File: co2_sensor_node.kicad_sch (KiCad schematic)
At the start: 27 parts, among them J1 Conn_01x03, J2 Conn_01x03, J3 Conn_01x02, J4 Conn_01x02, J5 Conn_01x03, J6 Conn_01x03

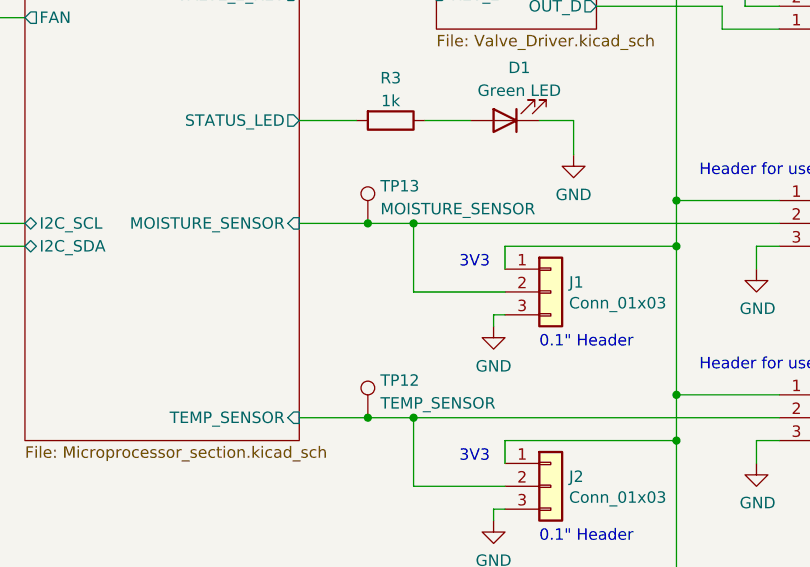
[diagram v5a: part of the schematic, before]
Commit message: Add voltage selection header for fan
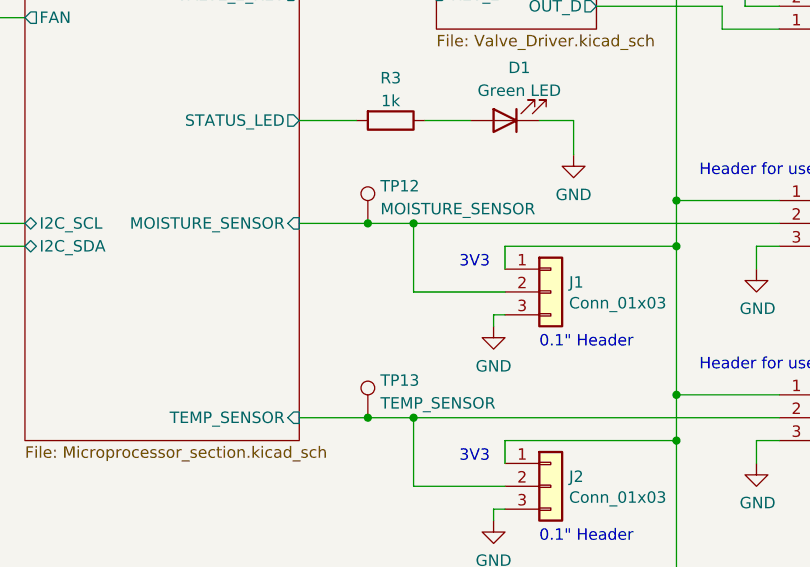
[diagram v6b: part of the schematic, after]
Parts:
- renumbered TP13 to TP12, TP12 to TP13
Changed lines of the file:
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@@
   (symbol (lib_id "Connector:TestPoint") (at 167.64 115.57 0) (unit 1)
     (in_bom yes) (on_board yes) (fields_autoplaced)
-    (property "Reference" "TP12" (id 0) (at 169.037 111.4333 0)
+    (property "Reference" "TP13" (id 0) (at 169.037 111.4333 0)
       (effects (font (size 1.27 1.27)) (justify left))
     )
@@
   (symbol (lib_id "Connector:TestPoint") (at 167.64 93.98 0) (unit 1)
     (in_bom yes) (on_board yes) (fields_autoplaced)
-    (property "Reference" "TP13" (id 0) (at 169.037 89.8433 0)
+    (property "Reference" "TP12" (id 0) (at 169.037 89.8433 0)
       (effects (font (size 1.27 1.27)) (justify left))
     )
@@
       (reference "#PWR039") (unit 1) (value "GND") (footprint "")
     )
+    (path "/00000000-0000-0000-0000-000060d4d720/a2b76130-4b73-41d2-b95d-ad9995d504d5"
+      (reference "#PWR040") (unit 1) (value "+BATT") (footprint "")
+    )
     (path "/00000000-0000-0000-0000-000060d4d720/00000000-0000-0000-0000-000060d47c8b"
-      (reference "#PWR040") (unit 1) (value "GND") (footprint "")
+      (reference "#PWR041") (unit 1) (value "GND") (footprint "")
     )
     (path "/1e0f6ce1-838d-48f3-88cf-c2592ace5fc7/78d904c8-e560-4928-a784-d6fb19cbf40d"
-      (reference "#PWR041") (unit 1) (value "GND") (footprint "")
+      (reference "#PWR042") (unit 1) (value "GND") (footprint "")
     )
     (path "/1e0f6ce1-838d-48f3-88cf-c2592ace5fc7/cbc2d777-8f3b-4a67-809c-e3f7baeb774b"
-      (reference "#PWR042") (unit 1) (value "GND") (footprint "")
+      (reference "#PWR043") (unit 1) (value "GND") (footprint "")
     )
     (path "/1e0f6ce1-838d-48f3-88cf-c2592ace5fc7/5cc37d78-3060-40cb-84bf-6df8015e864f"
-      (reference "#PWR043") (unit 1) (value "GND") (footprint "")
+      (reference "#PWR044") (unit 1) (value "GND") (footprint "")
     )
     (path "/1e0f6ce1-838d-48f3-88cf-c2592ace5fc7/b321f6d2-0341-4b1f-bee3-66cbe5374b62"
-      (reference "#PWR044") (unit 1) (value "GND") (footprint "")
+      (reference "#PWR045") (unit 1) (value "GND") (footprint "")
     )
     (path "/00000000-0000-0000-0000-000060a7e012/00000000-0000-0000-0000-000060a80f45"
-      (reference "#PWR045") (unit 1) (value "GND") (footprint "")
+      (reference "#PWR046") (unit 1) (value "GND") (footprint "")
     )
     (path "/00000000-0000-0000-0000-000060a7e012/00000000-0000-0000-0000-000060a81a13"
-      (reference "#PWR046") (unit 1) (value "GND") (footprint "")
+      (reference "#PWR047") (unit 1) (value "GND") (footprint "")
     )
     (path "/00000000-0000-0000-0000-000060ad9954/00000000-0000-0000-0000-000060ae7cec"
@@
       (reference "J11") (unit 1) (value "Conn_01x06_Male") (footprint "Connector_PinHeader_2.54mm:PinHeader_1x06_P2.54mm_Vertical")
     )
+    (path "/00000000-0000-0000-0000-000060d4d720/c5cd9f25-2ef9-4c26-8753-6b25093fa9df"
+      (reference "J12") (unit 1) (value "Conn_01x03") (footprint "Connector_PinHeader_2.54mm:PinHeader_1x03_P2.54mm_Vertical")
+    )
     (path "/00000000-0000-0000-0000-000060d4d720/00000000-0000-0000-0000-000060d47cab"
-      (reference "J12") (unit 1) (value "Conn_01x02") (footprint "co2_sensor_node:KF301-5.0-2P")
+      (reference "J13") (unit 1) (value "Conn_01x02") (footprint "co2_sensor_node:KF301-5.0-2P")
     )
     (path "/00000000-0000-0000-0000-000060a7e012/00000000-0000-0000-0000-000060b61966"
-      (reference "J13") (unit 1) (value "TF-15x15") (footprint "co2_sensor_node:TF-15x15")
+      (reference "J14") (unit 1) (value "TF-15x15") (footprint "co2_sensor_node:TF-15x15")
     )
     (path "/00000000-0000-0000-0000-000060a2751b/00000000-0000-0000-0000-000060aa0f54"
@@
       (reference "TP11") (unit 1) (value "GND") (footprint "TestPoint:TestPoint_Loop_D2.50mm_Drill1.0mm_LowProfile")
     )
+    (path "/a2566f92-d557-4d20-9a9b-690113e3c66e"
+      (reference "TP12") (unit 1) (value "MOISTURE_SENSOR") (footprint "TestPoint:TestPoint_Loop_D2.50mm_Drill1.0mm_LowProfile")
+    )
     (path "/98523834-76b6-42e0-866d-e4549b3c87a8"
-      (reference "TP12") (unit 1) (value "TEMP_SENSOR") (footprint "TestPoint:TestPoint_Loop_D2.50mm_Drill1.0mm_LowProfile")
-    )
-    (path "/a2566f92-d557-4d20-9a9b-690113e3c66e"
-      (reference "TP13") (unit 1) (value "MOISTURE_SENSOR") (footprint "TestPoint:TestPoint_Loop_D2.50mm_Drill1.0mm_LowProfile")
+      (reference "TP13") (unit 1) (value "TEMP_SENSOR") (footprint "TestPoint:TestPoint_Loop_D2.50mm_Drill1.0mm_LowProfile")
     )
     (path "/00000000-0000-0000-0000-000060ad9954/79553867-a79a-4b49-9db3-cf84d0d86e7b"

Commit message: Checkpoint
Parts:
- TP6: value CO2_RX -> CO2_TX
- TP7: value CO2_TX -> CO2_RX
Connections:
- net CO2 Sensor Connector/UART_RX: now also TP7.1; no longer TP6.1
- net CO2 Sensor Connector/UART_TX: now also TP6.1; no longer TP7.1
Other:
- sheet Microprocessor section ports: added none; removed CELL_1, CELL_2
- sheet Power ports: added none; removed CELL_1, CELL_2
- moved on the sheet: TP1
